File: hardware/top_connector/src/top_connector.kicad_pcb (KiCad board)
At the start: 2 copper layers, 38.5 x 28.5 mm, 14 parts, among them J1 to prev top connector, J2 to next top connector, J3 to module, U1 XL1509-5.0, U2 74LVC1G66

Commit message: Changed micro symbol to uF
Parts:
- C1: value 100µF -> 100uF
- C4: value 22µF -> 22uF
- L1: value 68µH -> 68uH
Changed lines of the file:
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@@
 		(property ki_fp_filters "SOT* SC*")
 		(sheetname "Root")
-		(sheetfile "Top Connector.kicad_sch")
+		(sheetfile "top_connector.kicad_sch")
 		(attr smd)
 		(fp_line
@@
 		(property ki_fp_filters "SOIC*3.9x4.9mm*P1.27mm*")
 		(sheetname "Root")
-		(sheetfile "Top Connector.kicad_sch")
+		(sheetfile "top_connector.kicad_sch")
 		(attr smd)
 		(fp_line
@@
 		(property ki_fp_filters "TO-???* *_Diode_* *SingleDiode* D_*")
 		(sheetname "Root")
-		(sheetfile "Top Connector.kicad_sch")
+		(sheetfile "top_connector.kicad_sch")
 		(attr smd)
 		(fp_line
@@
 			)
 		)
-		(property "Value" "68µH"
+		(property "Value" "68uH"
 			(at 0 4 0)
 			(layer "F.Fab")
@@
 		(property ki_fp_filters "Choke_* *Coil* Inductor_* L_*")
 		(sheetname "Root")
-		(sheetfile "Top Connector.kicad_sch")
+		(sheetfile "top_connector.kicad_sch")
 		(attr smd)
 		(fp_line
@@
 			)
 		)
-		(property "Value" "22µF"
+		(property "Value" "22uF"
 			(at 0 3.7 180)
 			(layer "F.Fab")
@@
 		(property ki_fp_filters "CP_*")
 		(sheetname "Root")
-		(sheetfile "Top Connector.kicad_sch")
+		(sheetfile "top_connector.kicad_sch")
 		(attr smd)
 		(fp_line
@@
 		(property ki_fp_filters "Connector*:*_2x??_*")
 		(sheetname "Root")
-		(sheetfile "Top Connector.kicad_sch")
+		(sheetfile "top_connector.kicad_sch")
 		(attr through_hole)
 		(fp_line
@@
 			)
 		)
-		(property "Value" "100µF"
+		(property "Value" "100uF"
 			(at 0 2.35 90)
 			(layer "F.Fab")
@@
 		(property ki_fp_filters "CP_*")
 		(sheetname "Root")
-		(sheetfile "Top Connector.kicad_sch")
+		(sheetfile "top_connector.kicad_sch")
 		(attr smd)
 		(fp_line
@@
 		(property ki_fp_filters "C_*")
 		(sheetname "Root")
-		(sheetfile "Top Connector.kicad_sch")
+		(sheetfile "top_connector.kicad_sch")
 		(attr smd)
 		(fp_line
@@
 		(property ki_fp_filters "MountingHole*")
 		(sheetname "Root")
-		(sheetfile "Top Connector.kicad_sch")
+		(sheetfile "top_connector.kicad_sch")
 		(attr exclude_from_pos_files exclude_from_bom)
 		(fp_circle
@@
 		(property ki_fp_filters "R_*")
 		(sheetname "Root")
-		(sheetfile "Top Connector.kicad_sch")
+		(sheetfile "top_connector.kicad_sch")
 		(attr smd)
 		(fp_line
@@
 		(property ki_fp_filters "Connector*:*_2x??_*")
 		(sheetname "Root")
-		(sheetfile "Top Connector.kicad_sch")
+		(sheetfile "top_connector.kicad_sch")
 		(attr smd)
 		(fp_line
@@
 		(property ki_fp_filters "Connector*:*_2x??_*")
 		(sheetname "Root")
-		(sheetfile "Top Connector.kicad_sch")
+		(sheetfile "top_connector.kicad_sch")
 		(attr through_hole)
 		(fp_line
@@
 		(property ki_fp_filters "C_*")
 		(sheetname "Root")
-		(sheetfile "Top Connector.kicad_sch")
+		(sheetfile "top_connector.kicad_sch")
 		(attr smd)
 		(fp_line

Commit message: update top connector to improve current path
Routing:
- net GND: track 167.1 -> 124.9 mm, vias 34 -> 29
- net +12V: track 82.0 -> 70.8 mm
- added copper zone on F.Cu, net +12V

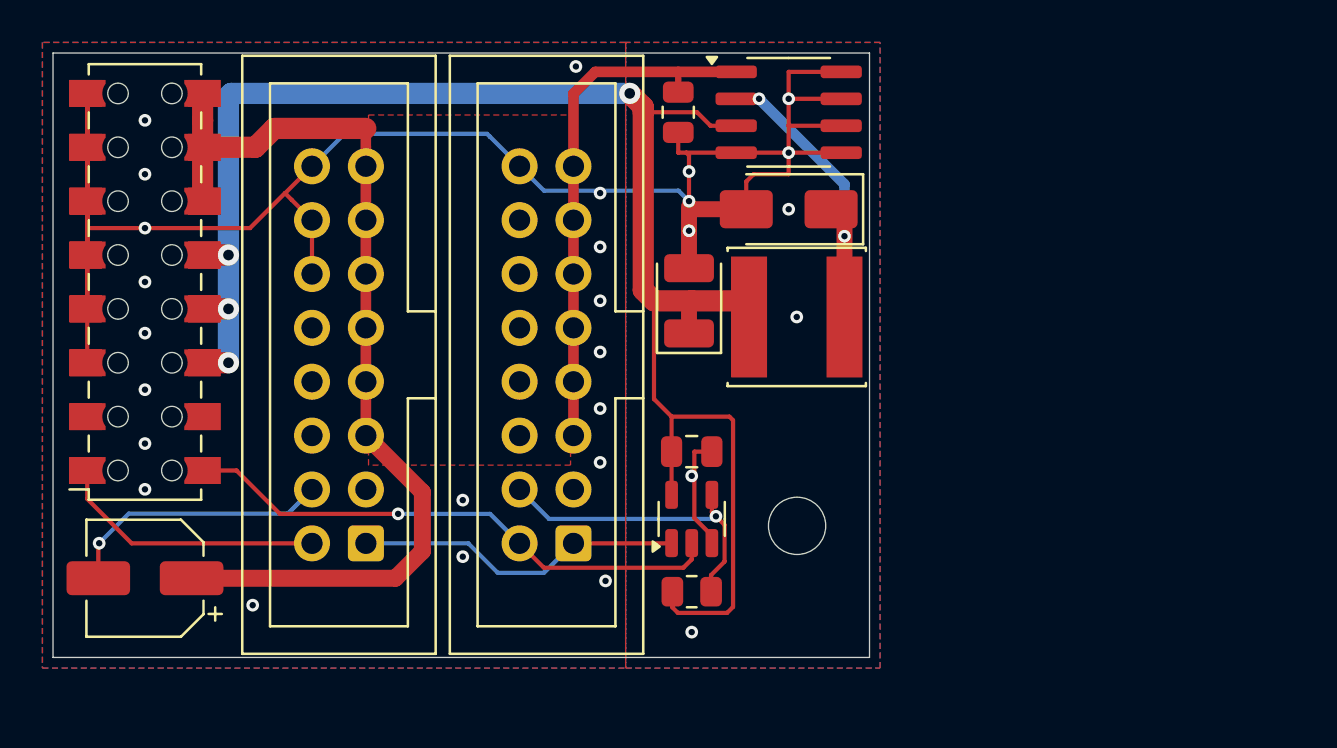
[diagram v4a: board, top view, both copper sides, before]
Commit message: Rework top connector and side panel connections to increase power rating. Switch from 2 channel to 4 channel incremental encoder.
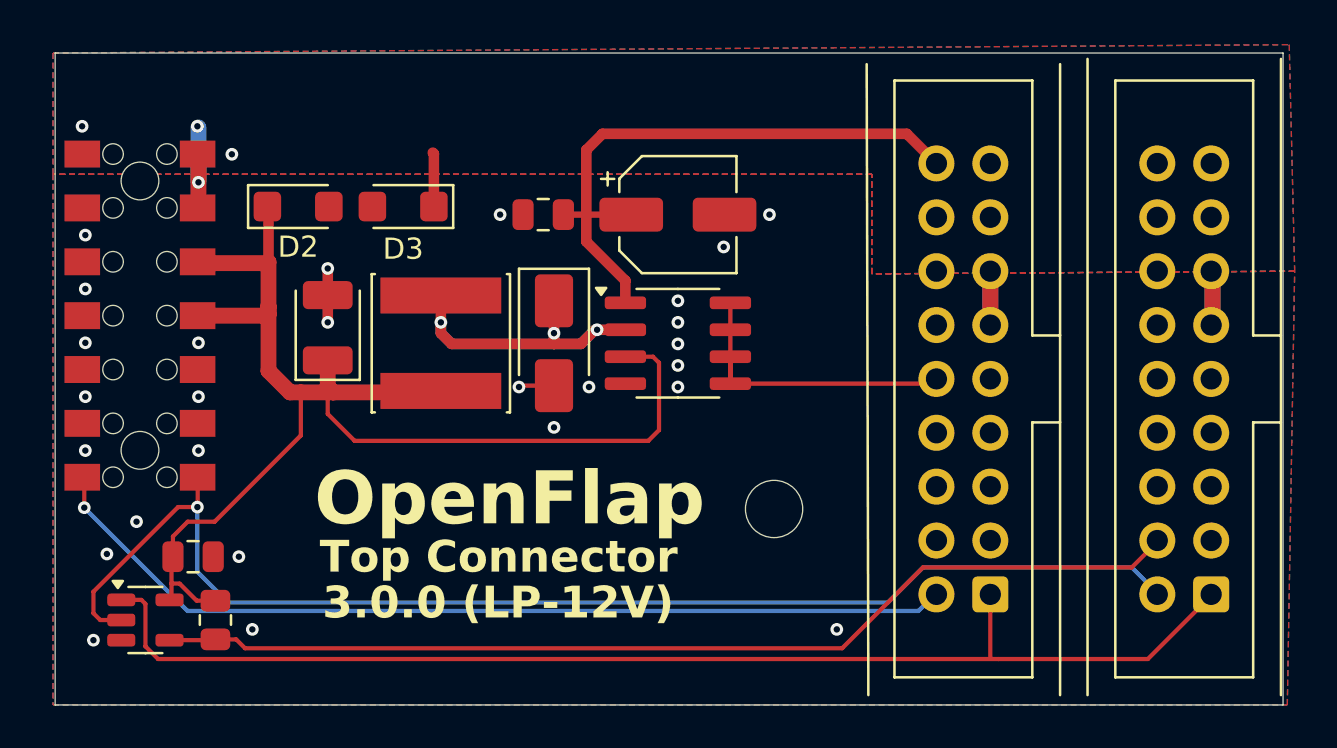
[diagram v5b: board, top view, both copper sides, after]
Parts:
- removed OSHW_LOGO_1: OSHW-Logo_5.7x6mm_SilkScreen, Symbol:OSHW-Logo_5.7x6mm_SilkScreen
- added D2: SMF5V0A, Diode_SMD:D_SMF, F.Cu at (97.7, 135.3)
- added D3: SMF12A, Diode_SMD:D_SMF, F.Cu at (102.6, 135.3)
- J1: value to prev top connector -> Conn_02x09_Odd_Even; footprint Connector_IDC:IDC-Header_2x08_P2.54mm_Vertical -> Connector_IDC:IDC-Header_2x09_P2.54mm_Vertical
- J2: value to next top connector -> Conn_02x09_Odd_Even; footprint Connector_IDC:IDC-Header_2x08_P2.54mm_Vertical -> Connector_IDC:IDC-Header_2x09_P2.54mm_Vertical
- J3: value to module -> Conn_02x07_Odd_Even; footprint Connector_Samtec_HLE_SMD:Samtec_HLE-108-02-xxx-DV-BE_2x08_P2.54mm_Horizontal -> Connector_Samtec_HLE_SMD:Samtec_HLE-107-02-xxx-DV-BE-A_2x07_P2.54mm_Horizontal
- moved C4 30.4 mm to (115.6, 135.7), turned to 0 degrees
- moved J2 30.2 mm to (140.7, 153.6)
- moved J1 29.5 mm to (130.3, 153.6)
- moved U2 26.2 mm to (90.5, 154.8), turned to 0 degrees
- moved C2 24.0 mm to (92.7, 151.8)
- moved R1 22.5 mm to (93.8, 154.8), turned to -90 degrees
- moved C1 17.1 mm to (99.1, 141.0)
- moved L1 16.8 mm to (104.4, 141.7), turned to -90 degrees
- moved D1 12.7 mm to (109.7, 141.7), turned to -90 degrees
- moved U1 12.1 mm to (115.6, 141.7)
- moved C3 7.99 mm to (109.2, 135.7), turned to 180 degrees
- moved J3 1.61 mm to (90.2, 140.4)
- moved H1 1.35 mm to (120.1, 149.6)
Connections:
- J1 pad 14: GND -> +12V
- J1 pad 16: GND -> +12V
- J1 pad 3: unconnected-(J1-Pin_3-Pad3) -> GND
- J1 pad 5: +12V -> GND
- J1 pad 7: +12V -> GND
- J1 pad 9: +12V -> GND
- J2 pad 14: GND -> +12V
- J2 pad 16: GND -> +12V
- J2 pad 3: unconnected-(J2-Pin_3-Pad3) -> GND
- J2 pad 5: +12V -> GND
- J2 pad 7: +12V -> GND
- J2 pad 9: +12V -> GND
- J3 pad 13: GND -> +12V
- J3 pad 3: unconnected-(J3-Pin_3-Pad3) -> GND
- J3 pad 4: unconnected-(J3-Pin_4-Pad4) -> GND
- J3 pad 6: +5V -> GND
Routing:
- net GND: track 124.9 -> 19.4 mm, vias 29 -> 27
- net /Data Return Path: track 15.4 -> 58.1 mm
- net /RX From Module: track 25.9 -> 60.7 mm
- net Net-(J2-Pin_4): track 15.1 -> 48.9 mm, vias 1 -> 0
- net /TX To Module: track 12.8 -> 44.0 mm, vias 0 -> 1
- net +12V: track 70.8 -> 46.0 mm, vias 0 -> 4
- net +5V: track 81.5 -> 62.6 mm, vias 4 -> 0
- net Net-(D1-K): track 15.1 -> 21.9 mm, vias 2 -> 3
- added copper zone on B.Cu, net +12V
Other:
- board size 38.5 x 28.5 mm -> 57.9 x 30.7 mm
- board text added: "${REVISION} (LP-12V)"
- board text removed: "${REVISION}"
